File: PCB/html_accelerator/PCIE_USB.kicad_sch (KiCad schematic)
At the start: 21 parts, among them U1 MCS9990, U2 AP1513

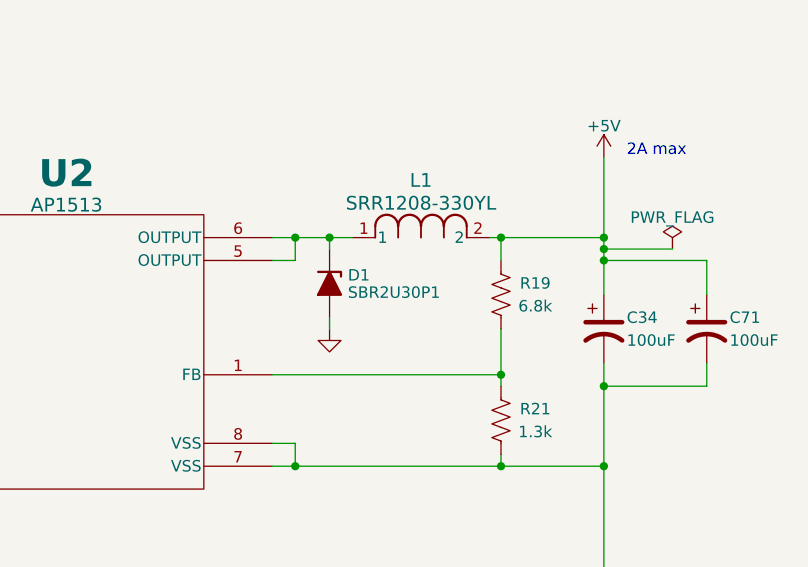
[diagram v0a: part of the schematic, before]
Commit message: update D1 footprint to correct bad symbol pin 1, new gerbers generated
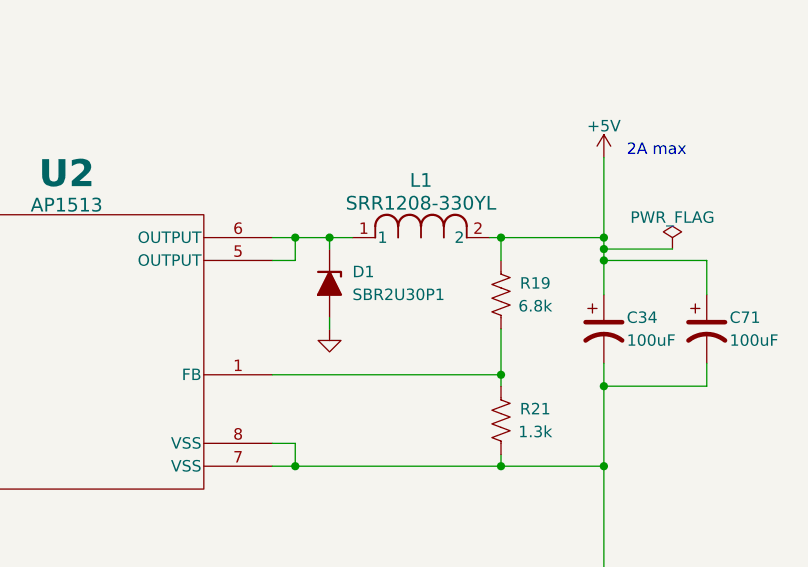
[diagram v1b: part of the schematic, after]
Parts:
- D1: footprint html_accel_footprints:DIODE_SBR3M30P1_1P78X2P8_DIO-M -> html_accel_footprints:DIODE_SBR2U30P1
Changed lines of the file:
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@@
 		(fields_autoplaced yes)
 		(property "Reference" "D1"
-			(at 120.142 148.9623 90)
+			(at 120.65 148.5899 90)
 			(show_name no)
 			(do_not_autoplace no)
@@
 		)
 		(property "Value" "SBR2U30P1"
-			(at 120.142 150.8833 90)
+			(at 120.65 151.1299 90)
 			(show_name no)
 			(do_not_autoplace no)
@@
 			)
 		)
-		(property "Footprint" "html_accel_footprints:DIODE_SBR3M30P1_1P78X2P8_DIO-M"
+		(property "Footprint" "html_accel_footprints:DIODE_SBR2U30P1"
 			(at 118.11 149.86 0)
 			(hide yes)
